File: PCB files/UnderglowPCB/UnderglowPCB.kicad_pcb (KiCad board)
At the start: 4 copper layers, 2 x 7.5 mm, 72 parts, among them J1 Screw_Terminal_01x03, J10 Screw_Terminal_01x03, J11 Conn_01x05, J12 Conn_01x07, J2 DB9_Male, J3 USB_B_Micro, J4 Screw_Terminal_01x03, J5 Screw_Terminal_01x03, J6 Screw_Terminal_01x03, J7 Screw_Terminal_01x03, J8 Screw_Terminal_01x03, J9 Screw_Terminal_01x03, Q1 S8050, Q2 S8050, U1 ESP32-WROOM-32D, U2 LMR14030-Q1, U3 NCP1117-3.3_SOT223, U4 74HC14, U5 74HC14, U6 SN65HVD230, U7 USBLC6-2SC6, U8 CP2102N-A01-GQFN28

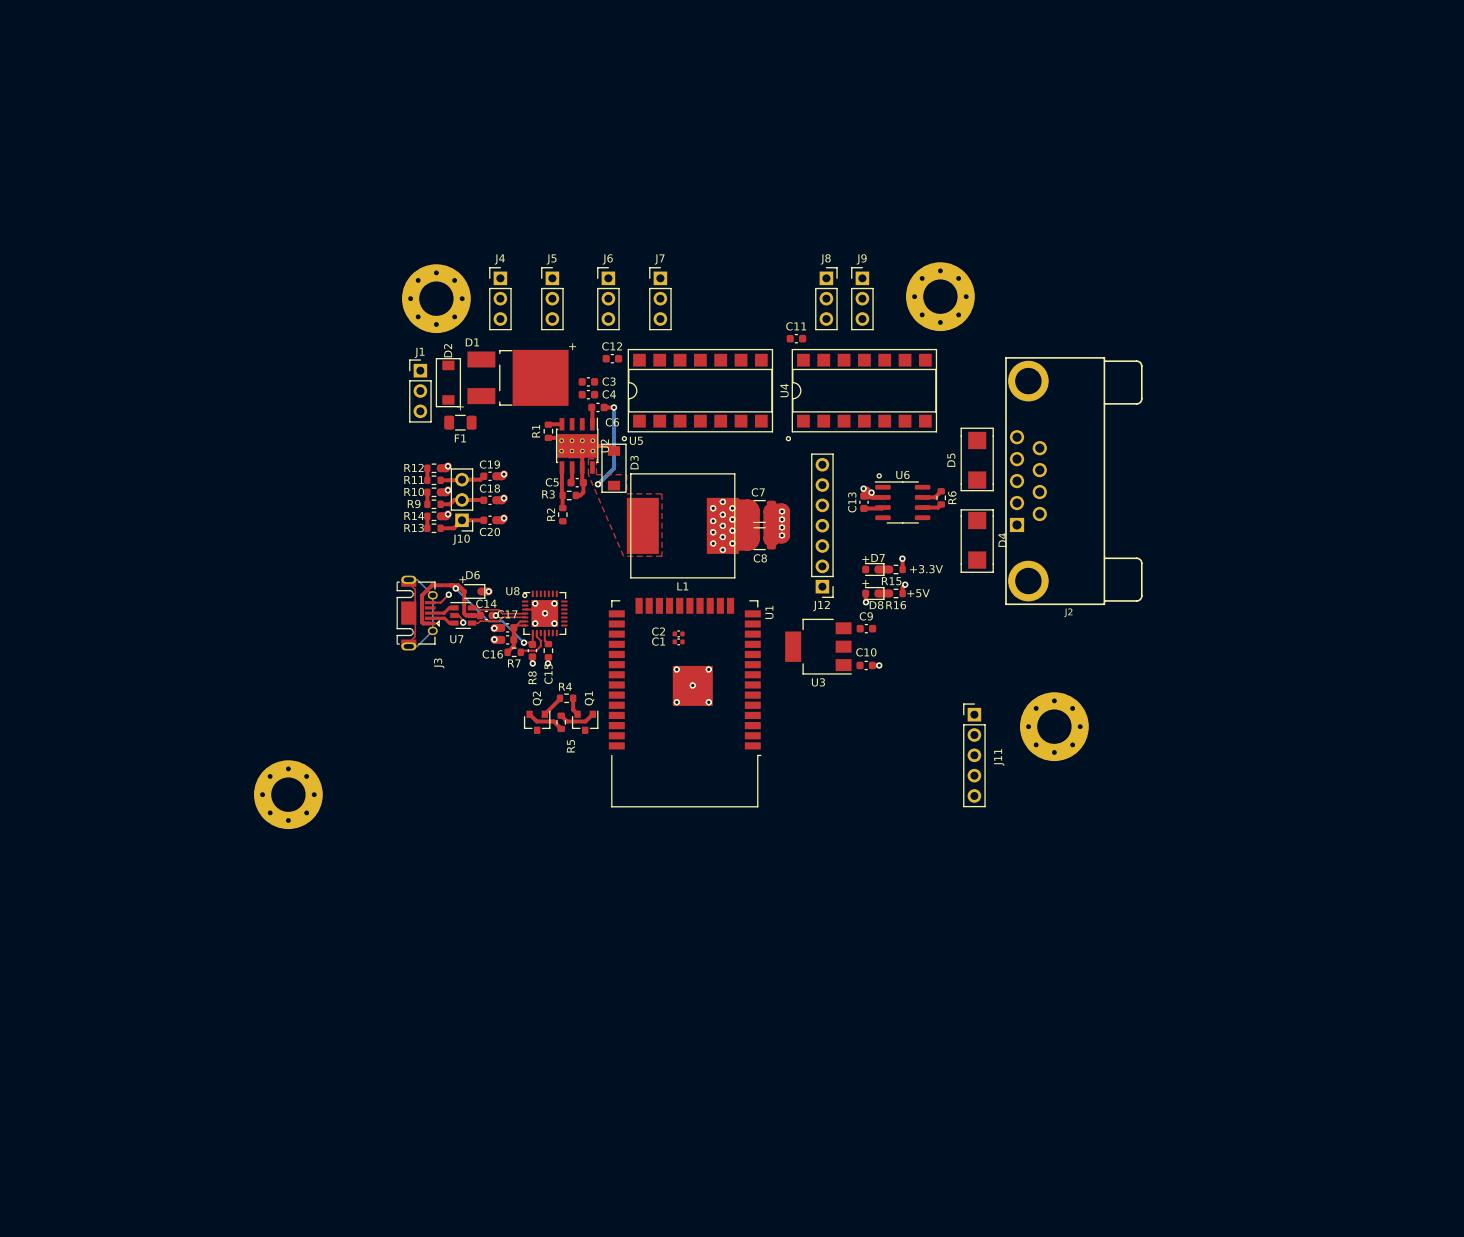
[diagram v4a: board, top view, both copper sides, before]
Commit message: PCB 1.2 finished. Needs some silkscreen work.
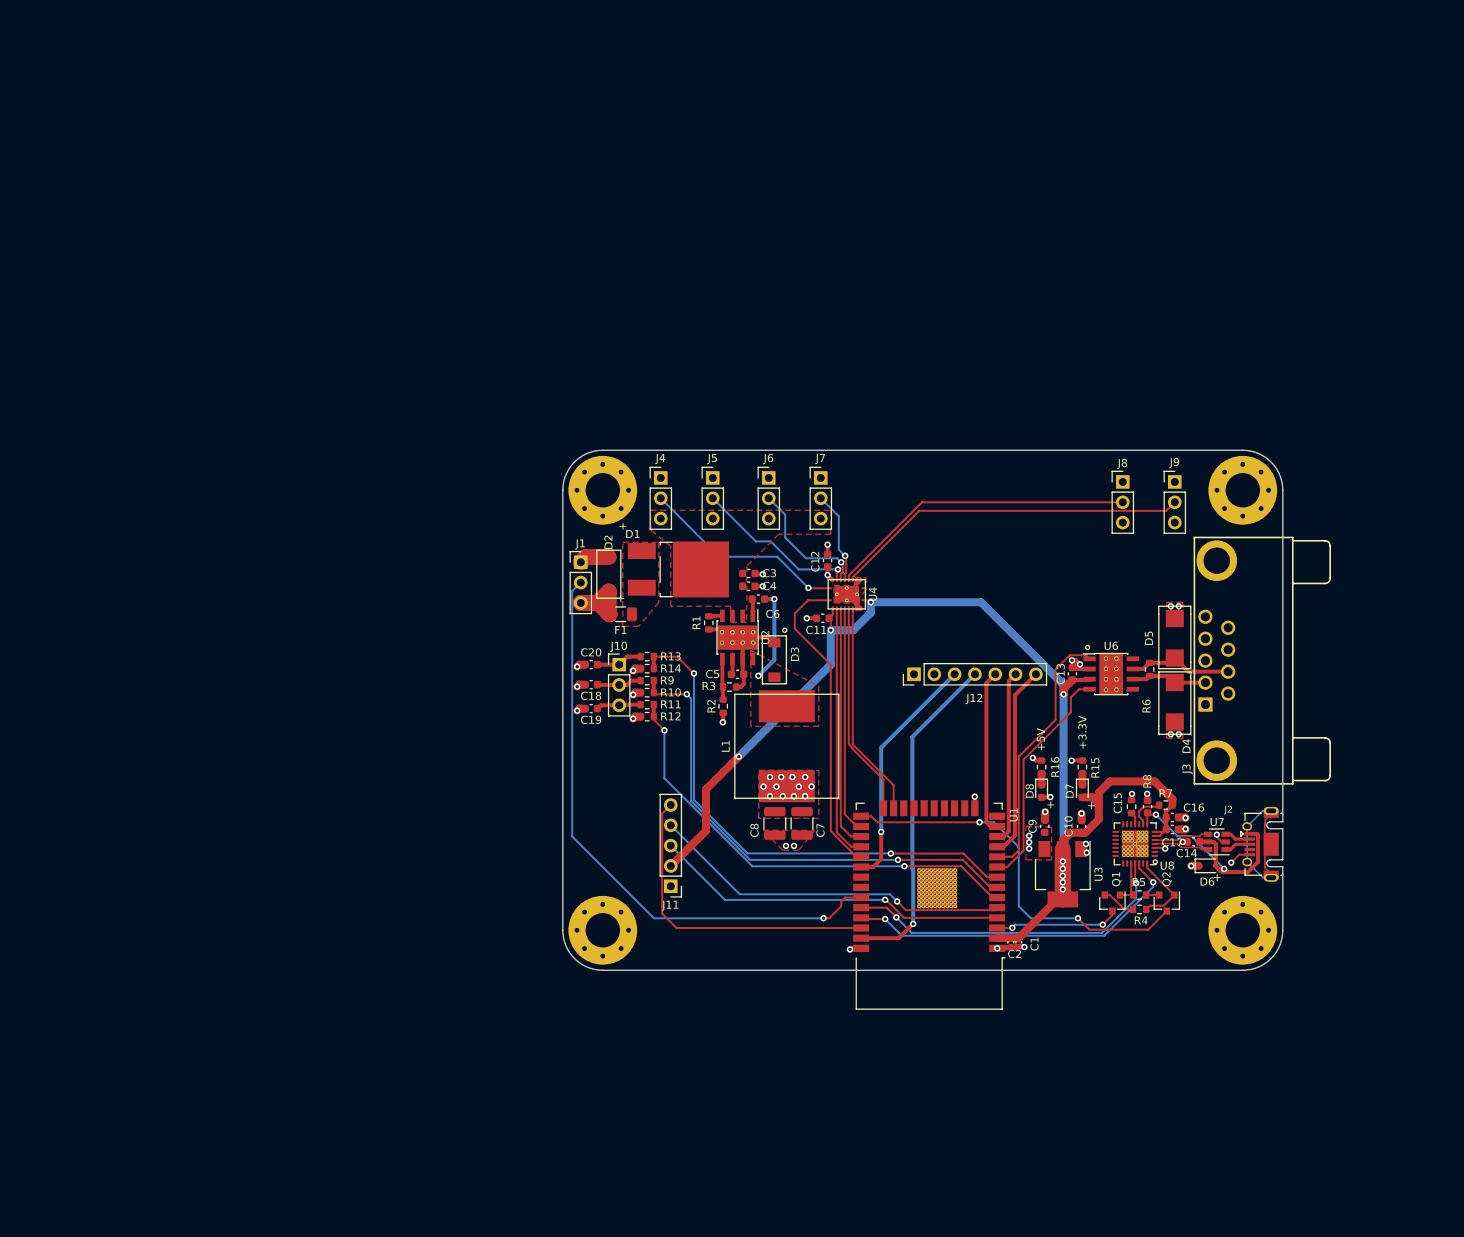
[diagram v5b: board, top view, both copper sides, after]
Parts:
- removed U5: 74HC14, Package_DIP:DIP-14_W7.62mm_SMDSocket_SmallPads
- C11, C12: value 10u -> 0.1u
- J11: footprint Connector_PinHeader_2.54mm:PinHeader_1x05_P2.54mm_Vertical -> UnderglowPCB:Joystick_Header
- J12: footprint Connector_PinHeader_2.54mm:PinHeader_1x07_P2.54mm_Vertical -> UnderglowPCB:SSD1306_Footprint
- J8: footprint Connector_PinSocket_2.54mm:PinSocket_1x03_P2.54mm_Vertical -> Connector_PinHeader_2.54mm:PinHeader_1x03_P2.54mm_Vertical
- U4: value 74HC14 -> TXB0108RGYR; footprint Package_DIP:DIP-14_W7.62mm_SMDSocket_SmallPads -> UnderglowPCB:VQFN-20
- U6: footprint Package_SO:SOIC-8_3.9x4.9mm_P1.27mm -> UnderglowPCB:Texas_HSOP-8-1EP_3.9x4.9mm_P1.27mm_ThermalVias
- moved J3 111.6 mm to (192.6, 117.2), turned to 90 degrees
- moved U7 98.4 mm to (185.8, 116.9), turned to 180 degrees
- moved D6 98.0 mm to (184.6, 119.9), turned to 0 degrees
- moved C14 92.8 mm to (182.9, 116.9), turned to 180 degrees
- moved C17 86.8 mm to (180.2, 115.3), turned to 0 degrees
- moved C16 86.0 mm to (180.2, 113.8), turned to 0 degrees
- moved R7 83.7 mm to (179.4, 112.3), turned to 0 degrees
- moved Q2 81.9 mm to (179.6, 124.5)
- moved C15 79.3 mm to (177.2, 112.5), turned to 90 degrees
- moved U8 79.2 mm to (175.6, 117.2), turned to 180 degrees
- moved R4 76.3 mm to (176.2, 125.3), turned to 0 degrees
- moved R8 75.5 mm to (175.2, 112.5), turned to 270 degrees
- moved R5 75.5 mm to (176.2, 123.5), turned to 180 degrees
- moved Q1 69.7 mm to (172.8, 124.5)
- moved C1 56.7 mm to (161.1, 129.4), turned to 270 degrees
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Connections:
- C11 pad 1: +5V -> +3V3
- J1 pad 2: Net-(J1-Pad2) -> AUX
- U1 pad 10: CAN_RX -> CAN_TX
- U1 pad 11: OLED_RESET -> OLED_CS
- U1 pad 13: OLED_CS -> OLED_RESET
- U1 pad 26: UG_LOW_FRONT -> UG_LOW_RIGHT
- U1 pad 28: UG_LOW_RIGHT -> UG_LOW_LEFT
- U1 pad 29: UG_LOW_LEFT -> UG_LOW_FRONT
- U1 pad 33: Net-(U1-Pad33) -> AUX
- U1 pad 4: JOYSTICK_Y -> JOYSTICK_X
- U1 pad 5: JOYSTICK_X -> JOYSTICK_Y
- U1 pad 6: BRAKE_LOW -> TURN_LEFT_LOW
- U1 pad 8: TURN_LEFT_LOW -> BRAKE_LOW
- U1 pad 9: CAN_TX -> CAN_RX
- U2 pad 3: Net-(U2-Pad3) -> +12V
- U4 pad 1: UG_LOW_RIGHT -> UG_LOW_FRONT
- U4 pad 10: 5V_LED_SPARE_1 -> +3V3
- U4 pad 11: Net-(U4-Pad11) -> GND
- U4 pad 12: UNDRGLW_RGHT -> GND
- U4 pad 13: Net-(U4-Pad13) -> GND
- U4 pad 14: +5V -> 5V_LED_SPARE_2
- U4 pad 2: Net-(U4-Pad13) -> +3V3
- U4 pad 3: UG_LOW_SPARE_2 -> UG_LOW_LEFT
- U4 pad 4: Net-(U4-Pad11) -> UG_LOW_REAR
- U4 pad 5: UG_LOW_SPARE_1 -> UG_LOW_RIGHT
- U4 pad 6: Net-(U4-Pad6) -> UG_LOW_SPARE_1
- U4 pad 7: GND -> UG_LOW_SPARE_2
- U4 pad 8: 5V_LED_SPARE_2 -> GND
- U4 pad 9: Net-(U4-Pad6) -> GND
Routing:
- net +3V3: track 9.12 -> 159.6 mm, vias 0 -> 9
- net AUX: track 0.00 -> 74.0 mm, vias 0 -> 1
- net BRAKE_LOW: track 1.50 -> 65.1 mm, vias 0 -> 2
- net TURN_RIGHT_LOW: track 1.50 -> 62.8 mm, vias 0 -> 2
- net TURN_LEFT_LOW: track 1.50 -> 57.5 mm, vias 0 -> 2
- net IO0: track 0.00 -> 49.4 mm, vias 0 -> 2
- net JOYSTICK_Y: track 0.00 -> 45.3 mm, vias 0 -> 1
- net JOYSTICK_X: track 0.00 -> 44.5 mm, vias 0 -> 1
- net 5V_LED_SPARE_2: track 0.00 -> 44.5 mm
- net TXD0: track 0.00 -> 43.6 mm, vias 0 -> 2
- net RXD0: track 0.00 -> 41.9 mm, vias 0 -> 2
- net MOSI: track 0.00 -> 41.7 mm, vias 0 -> 1
- net JOYSTICK_B: track 0.00 -> 39.6 mm
- net UG_LOW_FRONT: track 0.00 -> 39.2 mm
- net 5V_LED_SPARE_1: track 0.00 -> 38.6 mm
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- added copper zone on F.Cu, net +12V
- added copper zone on F.Cu, net +5V
- added copper zone on In2.Cu, net +5V
- added copper zone on F.Cu, net GND
- added copper zone on In1.Cu, net GND
- added copper zone on F.Cu, net Net-(D1-Pad2)
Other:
- board size 2 x 7.5 mm -> 90 x 65 mm
- board text added: "12V IN"
- board text added: "12V ONLY"
- board text added: "5V ONLY"
- board text added: "AUX PAD"
- board text added: "BRAKE"
- board text added: "LEFT TURN SIGNAL"
- board text added: "RIGHT TURN SIGNAL"
- board text added: "SSD1306"
- board text removed: "12V TEST POINT"
- board text removed: "3.3V TEST POINT"
- board text removed: "5V TEST POINT"
- board text removed: "SCREEN"

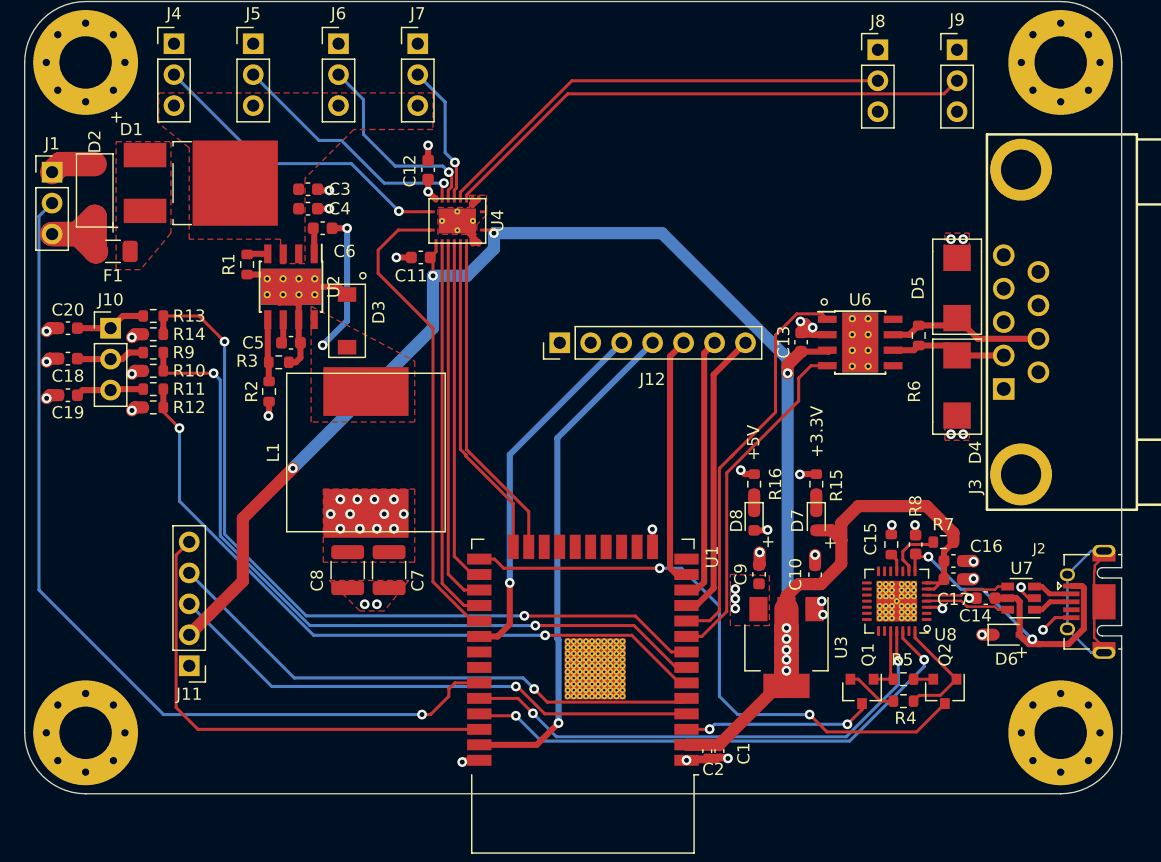
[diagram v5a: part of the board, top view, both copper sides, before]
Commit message: PCB Ver 1.3.2 completed. Documentaion updated to reflect changes. BOM Added to Hardware.md
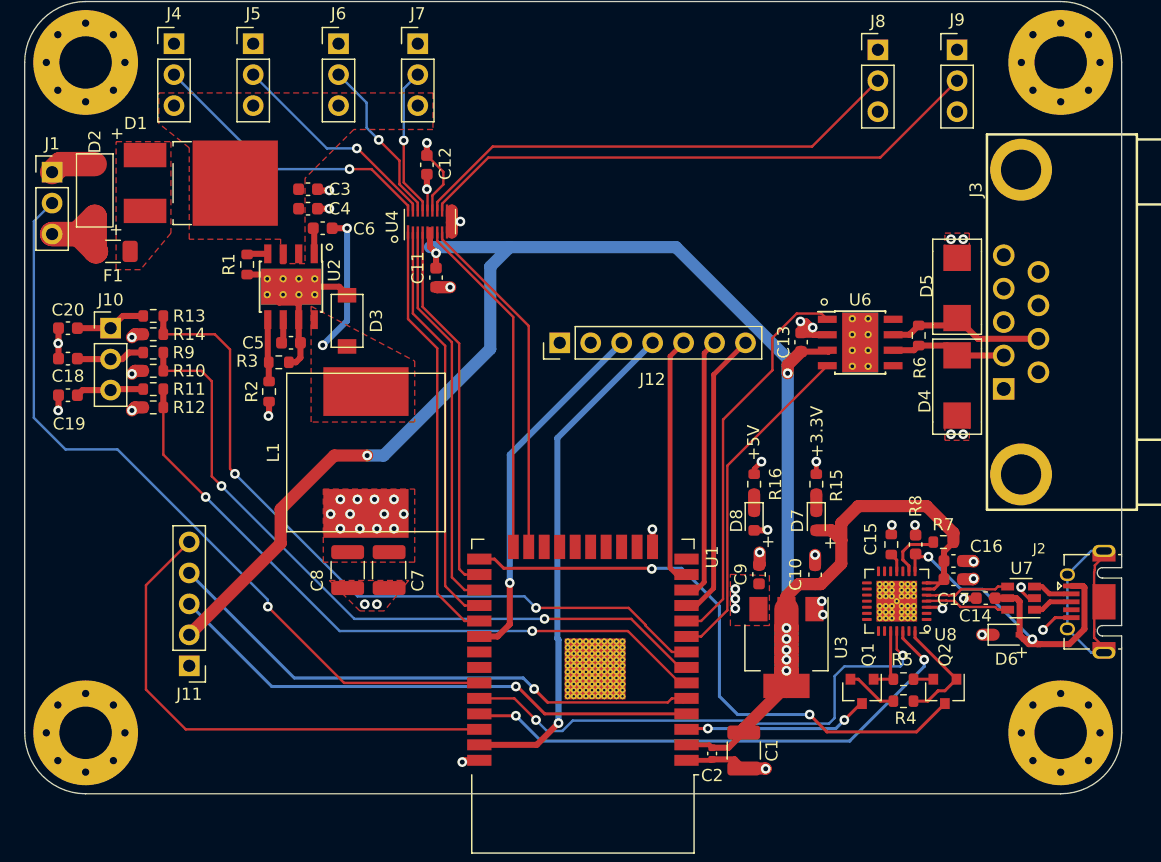
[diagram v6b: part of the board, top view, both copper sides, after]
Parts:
- C1: footprint Capacitor_SMD:C_0402_1005Metric -> Capacitor_SMD:C_1210_3225Metric
- C14, C6: value .1u -> 0.1u
- D3: footprint UnderglowPCB:TPSMA6L15A -> UnderglowPCB:DO-221AC
- D6: value BAT760-7 -> B5818WS
- J1, J10, J4, J5, J6, J7, J8, J9: value Screw_Terminal_01x03 -> Conn_01x03
- U4: value TXB0108RGYR -> TXB0108DQSR; footprint UnderglowPCB:VQFN-20 -> Package_SON:USON-20_2x4mm_P0.4mm
- moved U4 2.25 mm to (137.3, 86.0)
- moved C11 2.07 mm to (137.8, 90.6), turned to 90 degrees
- moved C1 2.00 mm to (163.1, 129.4)
- moved C2 0.45 mm to (160.4, 129.7)
- moved C12 0.41 mm to (137.1, 81.3), turned to 270 degrees
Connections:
- C11 pad 1: +3V3 -> GND
- C11 pad 2: GND -> +3V3
- C12 pad 1: +5V -> GND
- C12 pad 2: GND -> +5V
- U4 pad 10: +3V3 -> GND
- U4 pad 13: GND -> 5V_LED_SPARE_2
- U4 pad 14: 5V_LED_SPARE_2 -> 5V_LED_SPARE_1
- U4 pad 15: 5V_LED_SPARE_1 -> GND
- U4 pad 16: UNDRGLW_RGHT -> +5V
- U4 pad 17: UNDRGLW_REAR -> UNDRGLW_RGHT
- U4 pad 18: UNDRGLW_LEFT -> UNDRGLW_REAR
- U4 pad 19: +5V -> UNDRGLW_LEFT
- U4 pad 2: +3V3 -> UG_LOW_LEFT
- U4 pad 3: UG_LOW_LEFT -> UG_LOW_REAR
- U4 pad 4: UG_LOW_REAR -> UG_LOW_RIGHT
- U4 pad 5: UG_LOW_RIGHT -> +3V3
- U4 pad 6: UG_LOW_SPARE_1 -> +3V3
- U4 pad 7: UG_LOW_SPARE_2 -> UG_LOW_SPARE_1
- U4 pad 8: GND -> UG_LOW_SPARE_2
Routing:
- net AUX: track 74.0 -> 64.1 mm
- net UG_LOW_FRONT: track 39.2 -> 35.1 mm
- net BRAKE_LOW: track 65.1 -> 61.0 mm
- net +3V3: track 159.6 -> 162.8 mm, vias 9 -> 8
- net TURN_RIGHT_LOW: track 62.8 -> 59.8 mm
- net UNDRGLW_LEFT: track 20.7 -> 18.0 mm
- net JOYSTICK_B: track 39.6 -> 42.3 mm
- net UNDRGLW_REAR: track 16.4 -> 13.8 mm
- net 5V_LED_SPARE_2: track 44.5 -> 47.0 mm
- net 5V_LED_SPARE_1: track 38.6 -> 41.0 mm
- net UG_LOW_RIGHT: track 28.4 -> 30.7 mm
- net GND: track 70.5 -> 72.5 mm, vias 36 -> 35
- net UG_LOW_REAR: track 30.3 -> 32.1 mm
- net UG_LOW_LEFT: track 31.8 -> 33.6 mm
- net UNDRGLW_FRNT: track 25.8 -> 24.1 mm
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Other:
- net class Default: clearance 0.1 -> 0.15
- rule trace_clearance: 0.1 -> 0.15
